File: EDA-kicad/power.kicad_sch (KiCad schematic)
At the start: 99 parts, among them SW1 EG25-switch-CSS-1210MC, SW2 MIC-switch-CSS-1210MC, SW3 CAM-switch-CSS-1210MC, U11 TPS65023BRSBR, U4 BQ25792RQMR, U6 BAT-CONNECTOR-FLTS22WR00, U7 22V-boost-AP3032KTR-G1, U8 MP3429GL-Z

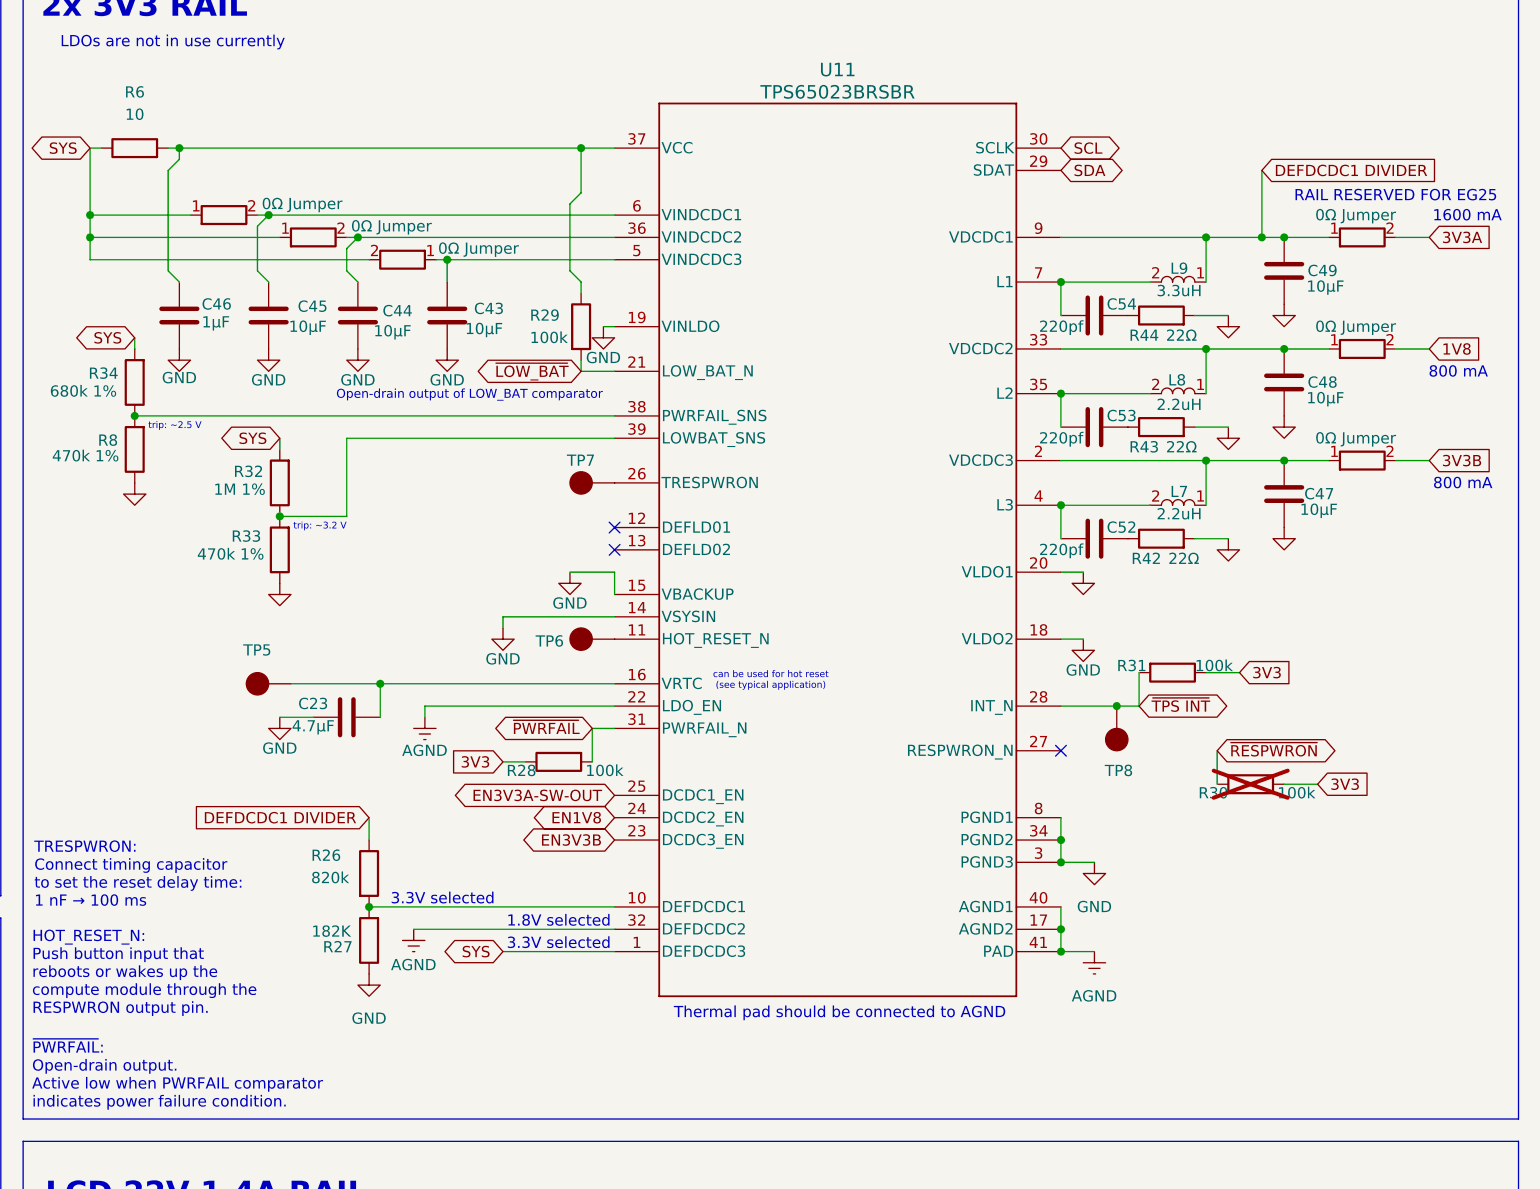
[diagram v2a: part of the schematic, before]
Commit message: remove snubbers, leave note, improve clarity
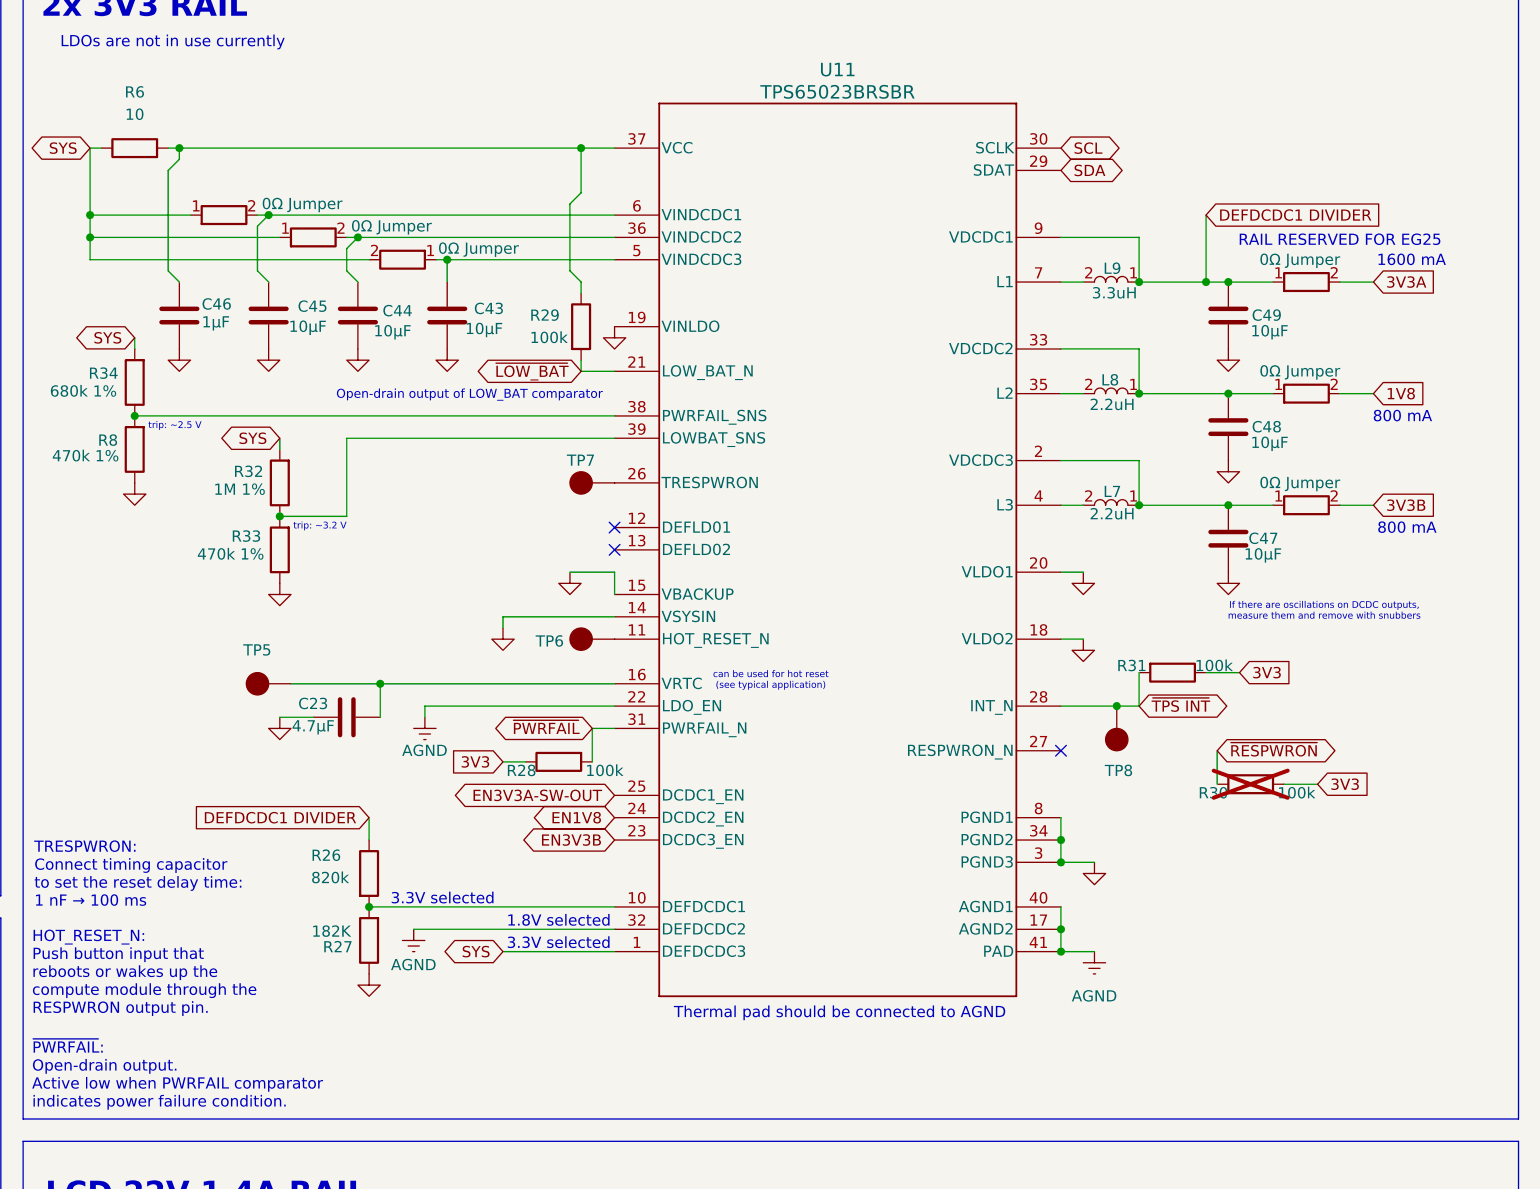
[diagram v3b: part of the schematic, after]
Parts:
- removed C52, C53, C54: 220pf, SPIRIT-footprints:0603-capacitor, symbol Device:C
- removed R42, R43, R44: 22Ω, SPIRIT-footprints:0603-resistor, symbol Device:R
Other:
- note added: "If there are oscillations on DCDC outputs, measure them and remove with snubbers"
- moved on the sheet: C47, C48, C49, L7, L8, L9

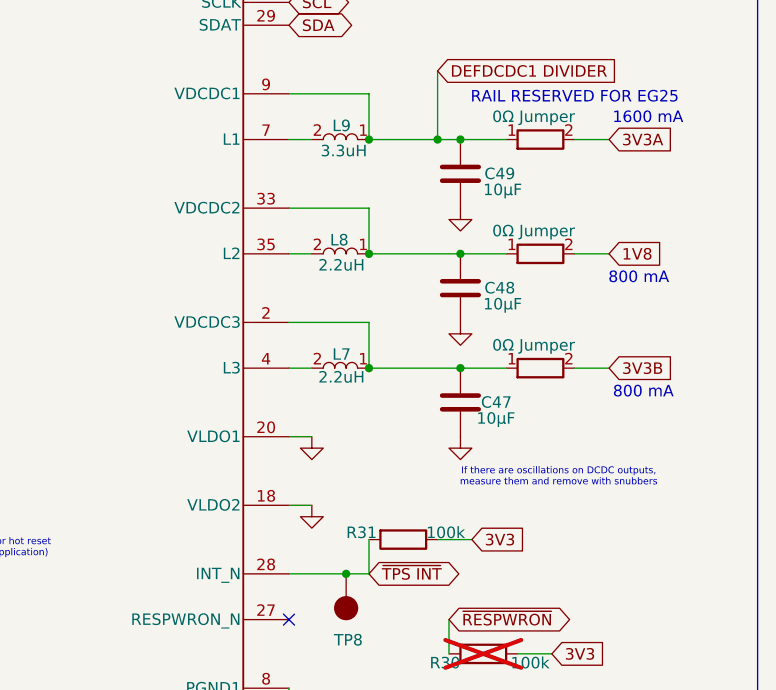
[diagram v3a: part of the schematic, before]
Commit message: fix wrong capacitors on DCDC output
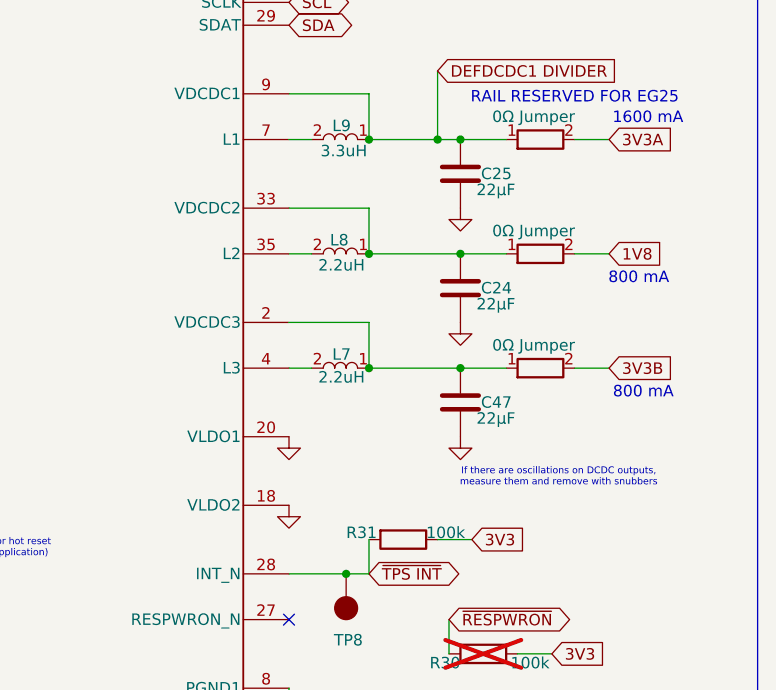
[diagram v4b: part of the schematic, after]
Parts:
- removed C48, C49: 10μF, SPIRIT-footprints:0603-capacitor, symbol Device:C
- C47: value 10μF -> 22μF; MPN CC0603KRX5R6BB106 -> CC0603MRX6S5BB226
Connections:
- net DEFDCDC1 DIVIDER: now also C47.1
- net at L8.1, R36.1, U11.33 (VDCDC2): now also C47.1
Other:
- moved on the sheet: C24

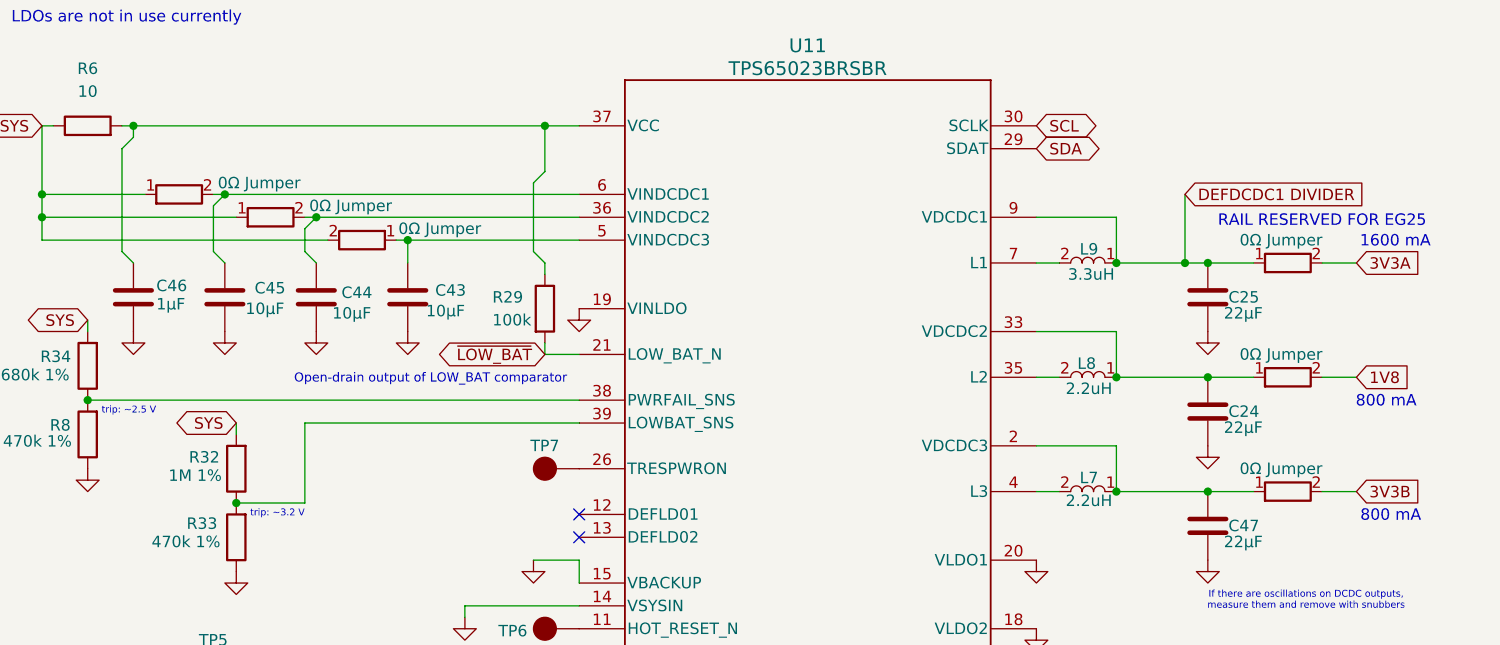
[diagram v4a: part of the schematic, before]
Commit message: Add MPN to 0 Ohm jumper symbols, shorten text
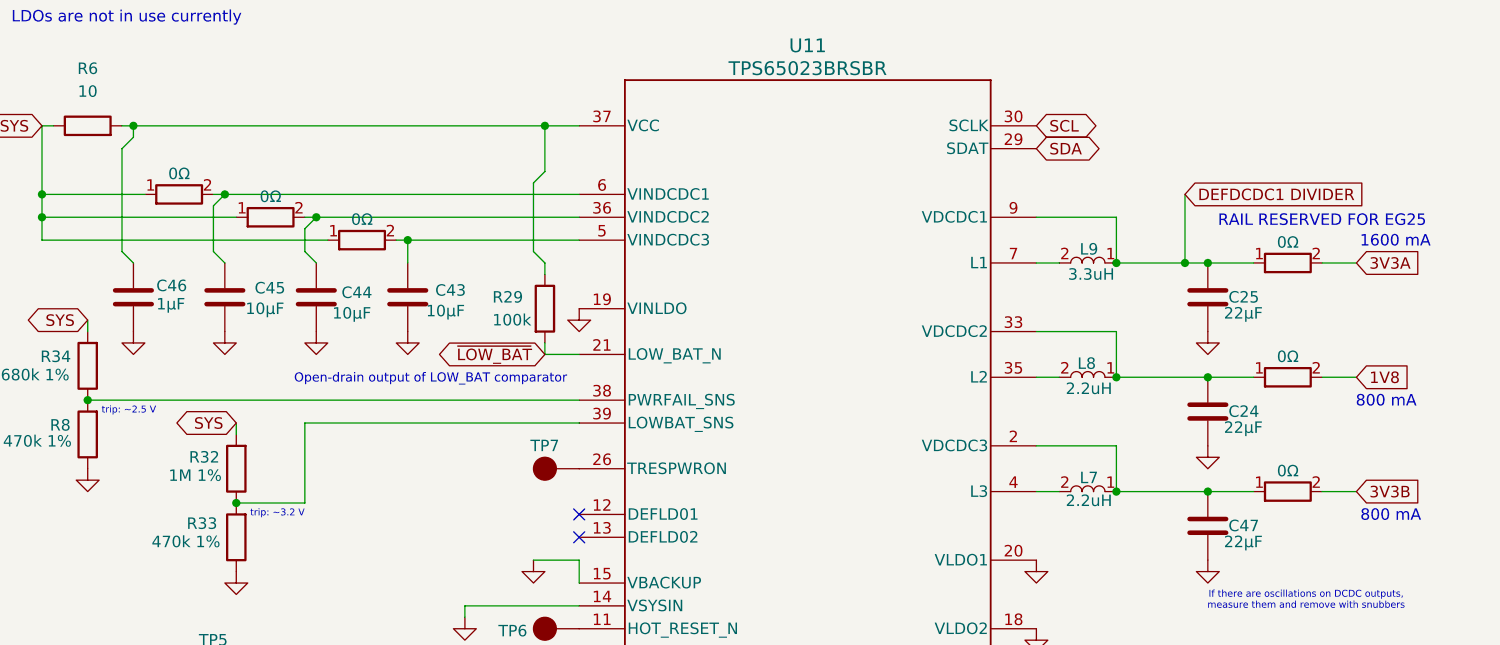
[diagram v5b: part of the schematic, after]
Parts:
- removed R35, R36, R39, R40, R41: 0Ω Jumper, SPIRIT-footprints:1K-05W-0805-RES_ERJP06J102V, symbol SPIRIT-components:1K-05W-0805-RES_ERJP06J102V
- R11: renamed from R37; value 0Ω Jumper -> 0Ω; MANUFACTURER Panasonic -> (none); MAXIMUM_PACKAGE_HEIGHT 0.6 mm -> (none); MPN (none) -> RC0805JR-070RL; PARTREV 3/1/2020 -> (none); STANDARD Manufacturer Recommendations -> (none)
- renumbered C47 to C25
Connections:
- net 1V8: now also R11.2
- net 3V3A: now also R11.2
- net DEFDCDC1 DIVIDER: now also R11.1
- net SYS: now also R11.1
- net at C45.1, U11.6 (VINDCDC1): now also R11.2
- net at C25.1, L8.1, U11.33 (VDCDC2): now also R11.1
- net at C43.1, U11.5 (VINDCDC3): now also R11.2
- net at C44.1, U11.36 (VINDCDC2): now also R11.2
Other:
- moved on the sheet: C47

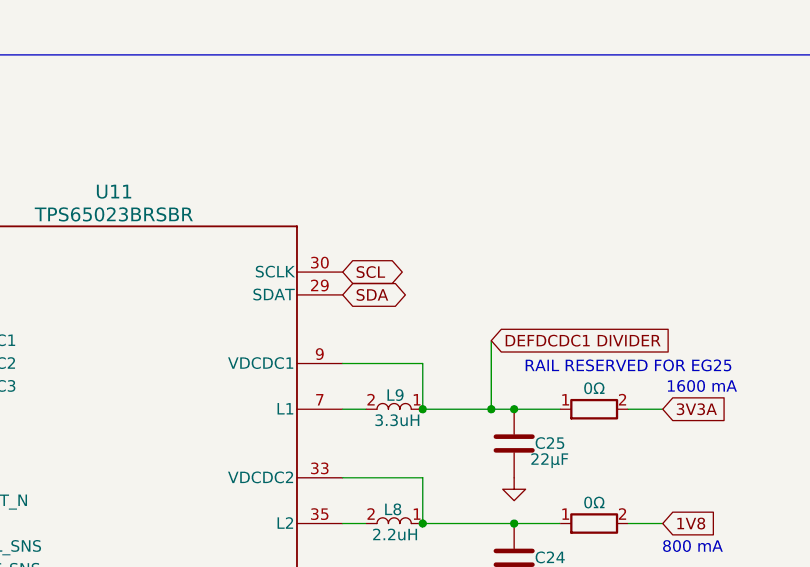
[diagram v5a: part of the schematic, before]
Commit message: connect PMIC I2C to CM5
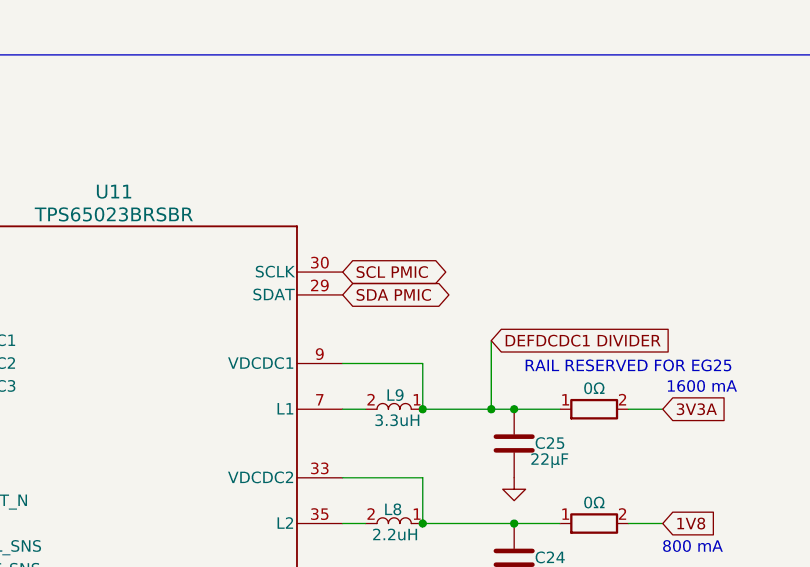
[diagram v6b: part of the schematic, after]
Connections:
- net SCL: no longer U11.30 (SCLK)
- net SDA: no longer U11.29 (SDAT)
- new net SCL PMIC: U11.30 (SCLK)
- new net SDA PMIC: U11.29 (SDAT)
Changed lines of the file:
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@@
 		)
 	)
-	(global_label "SDA"
+	(global_label "SDA PMIC"
 		(shape bidirectional)
 		(at 354.33 77.47 0)
@@
 		)
 		(property "Intersheetrefs" "${INTERSHEET_REFS}"
-			(at 361.9946 77.47 0)
+			(at 367.5584 77.47 0)
 			(effects
 				(font
@@
 		)
 	)
-	(global_label "SCL"
+	(global_label "SCL PMIC"
 		(shape bidirectional)
 		(at 354.33 74.93 0)
@@
 		)
 		(property "Intersheetrefs" "${INTERSHEET_REFS}"
-			(at 361.9341 74.93 0)
-			(effects
-				(font
+			(at 367.4979 74.93 0)
+			(effects
+				(font

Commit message: Updated values of passive components
Updated values of passive components (resistors and capacitors) to include Ohm symbol, and removed microfarads symbol replaced by "uf" to fix BOM generator confusion.
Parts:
- added C24, C25: 22uF, SPIRIT-footprints:0603-capacitor, symbol Device:C
- added R10, R11, R12, R35, R36: 0Ω, SPIRIT-footprints:1K-05W-0805-RES_ERJP06J102V, symbol SPIRIT-components:1K-05W-0805-RES_ERJP06J102V
- C10, C23, C41: value 4.7μF -> 4.7uF
- C11, C17, C32, C36: value 0.1μF -> 0.1uF
- C12, C13, C14, C18, C19, C20, C21, C22, C43, C44, C45, C7, C8: value 10μF -> 10uF
- C30, C31, C46: value 1μF -> 1uF
- C33, C34, C35, C37, C38, C39, C42: value 22μF -> 22uF
- C47: renamed from C25; value 22μF -> 22uF
- R13: value 5.23k -> 5.23kΩ
- R14, R15, R18: value 10k -> 10kΩ
- R16: value 30k -> 30kΩ
- R17: value 680 -> 680Ω
- R20: value 5 -> 5Ω
- R21: value 750k -> 750kΩ
- R22: value 200k -> 200kΩ
- R23: value 6.8k -> 6.8kΩ
- R26: value 820k -> 820kΩ
- R27: value 182K -> 182KΩ
- R28, R29, R30, R31, R7: value 100k -> 100kΩ
- R32: value 1M 1% -> 1MΩ 1%
- R33, R8: value 470k 1% -> 470kΩ 1%
- R34: value 680k 1% -> 680kΩ 1%
- R4: value 127k -> 127kΩ
- R5: value 4.7K -> 4.7KΩ
- R6: value 10 -> 10Ω
- R9: value 100 -> 100Ω
- renumbered R11 to R37
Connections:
- net 1V8: now also R10.2; no longer R37.2
- net 3V3A: now also R11.2; no longer R37.2
- net DEFDCDC1 DIVIDER: now also C25.1, R11.1; no longer C47.1, R37.1
- net GND: now also C24.2, C25.2
- net SYS: now also R12.1, R35.1, R36.1; no longer R37.1
- net at L8.1, U11.33 (VDCDC2): now also C24.1, R10.1; no longer C47.1, R37.1
- net at C45.1, U11.6 (VINDCDC1): now also R12.2; no longer R37.2
- net at C43.1, U11.5 (VINDCDC3): now also R36.2; no longer R37.2
- net at C44.1, U11.36 (VINDCDC2): now also R35.2; no longer R37.2
